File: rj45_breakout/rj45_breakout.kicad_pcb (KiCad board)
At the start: 2 copper layers, 74.3 x 80.6 mm, 19 parts, among them J10 Conn_01x08, J6 RJ45_Shielded, J9 Conn_02x04_Odd_Even

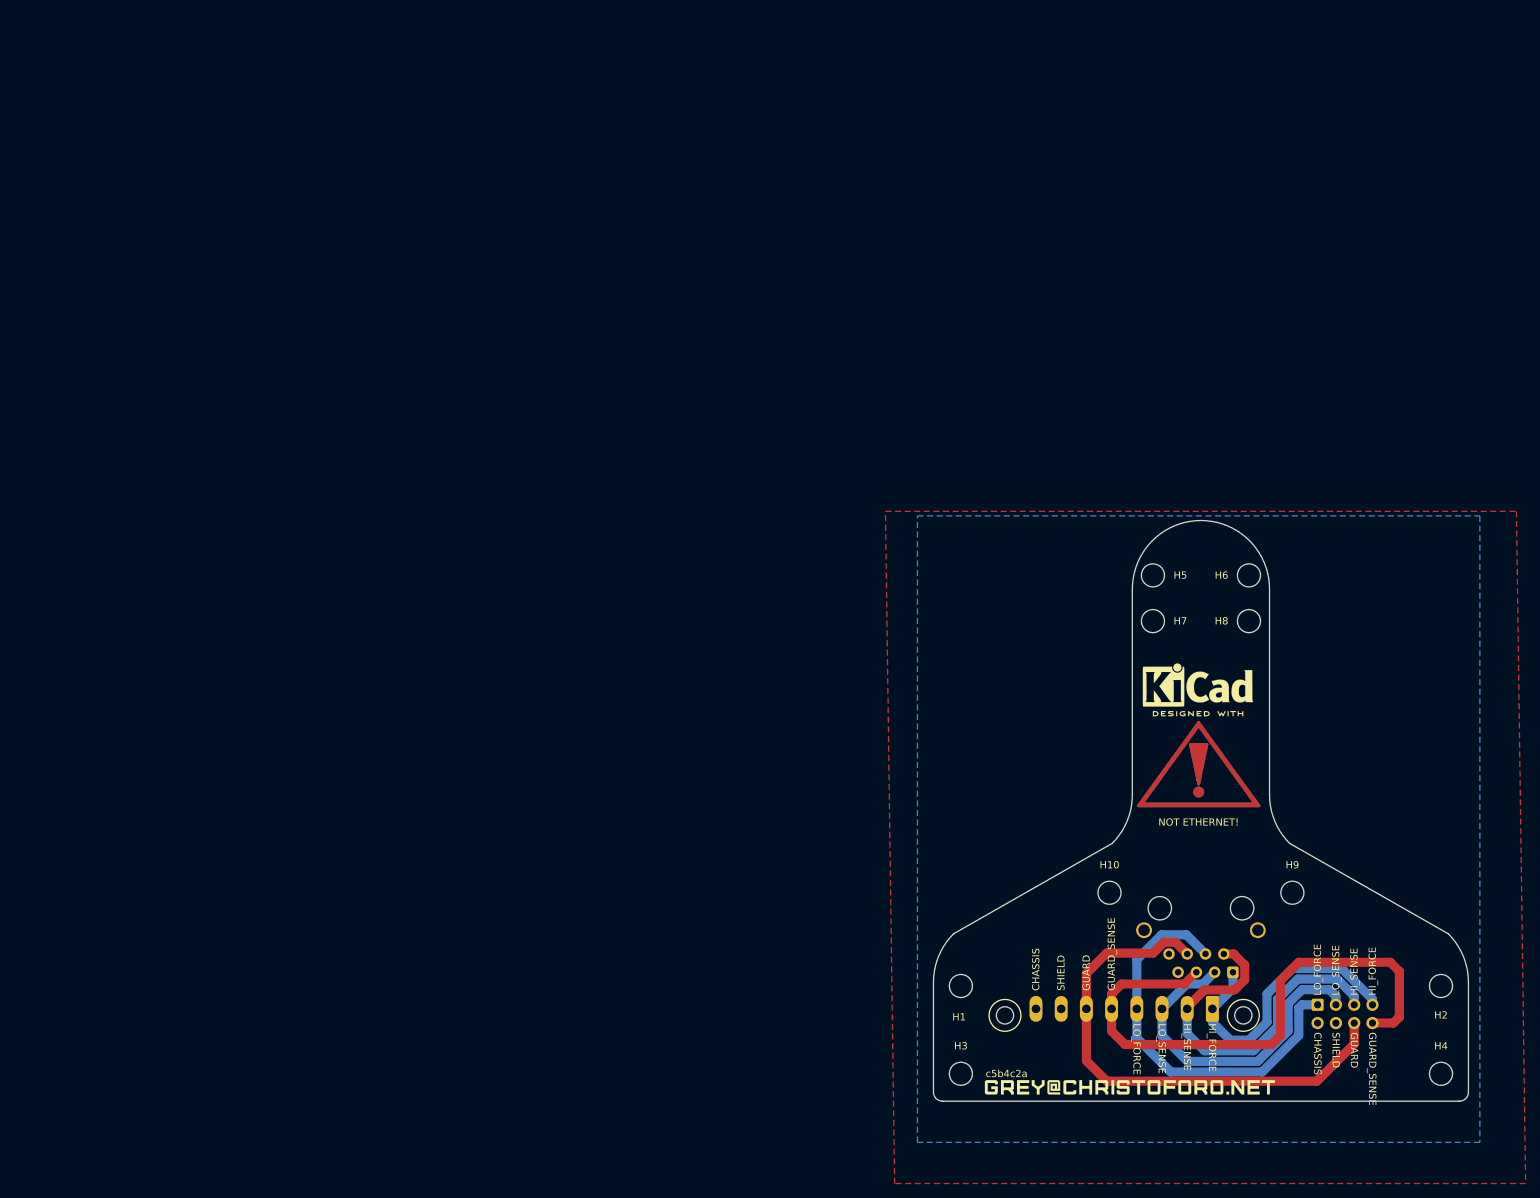
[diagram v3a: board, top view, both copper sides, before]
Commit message: move connector to edge
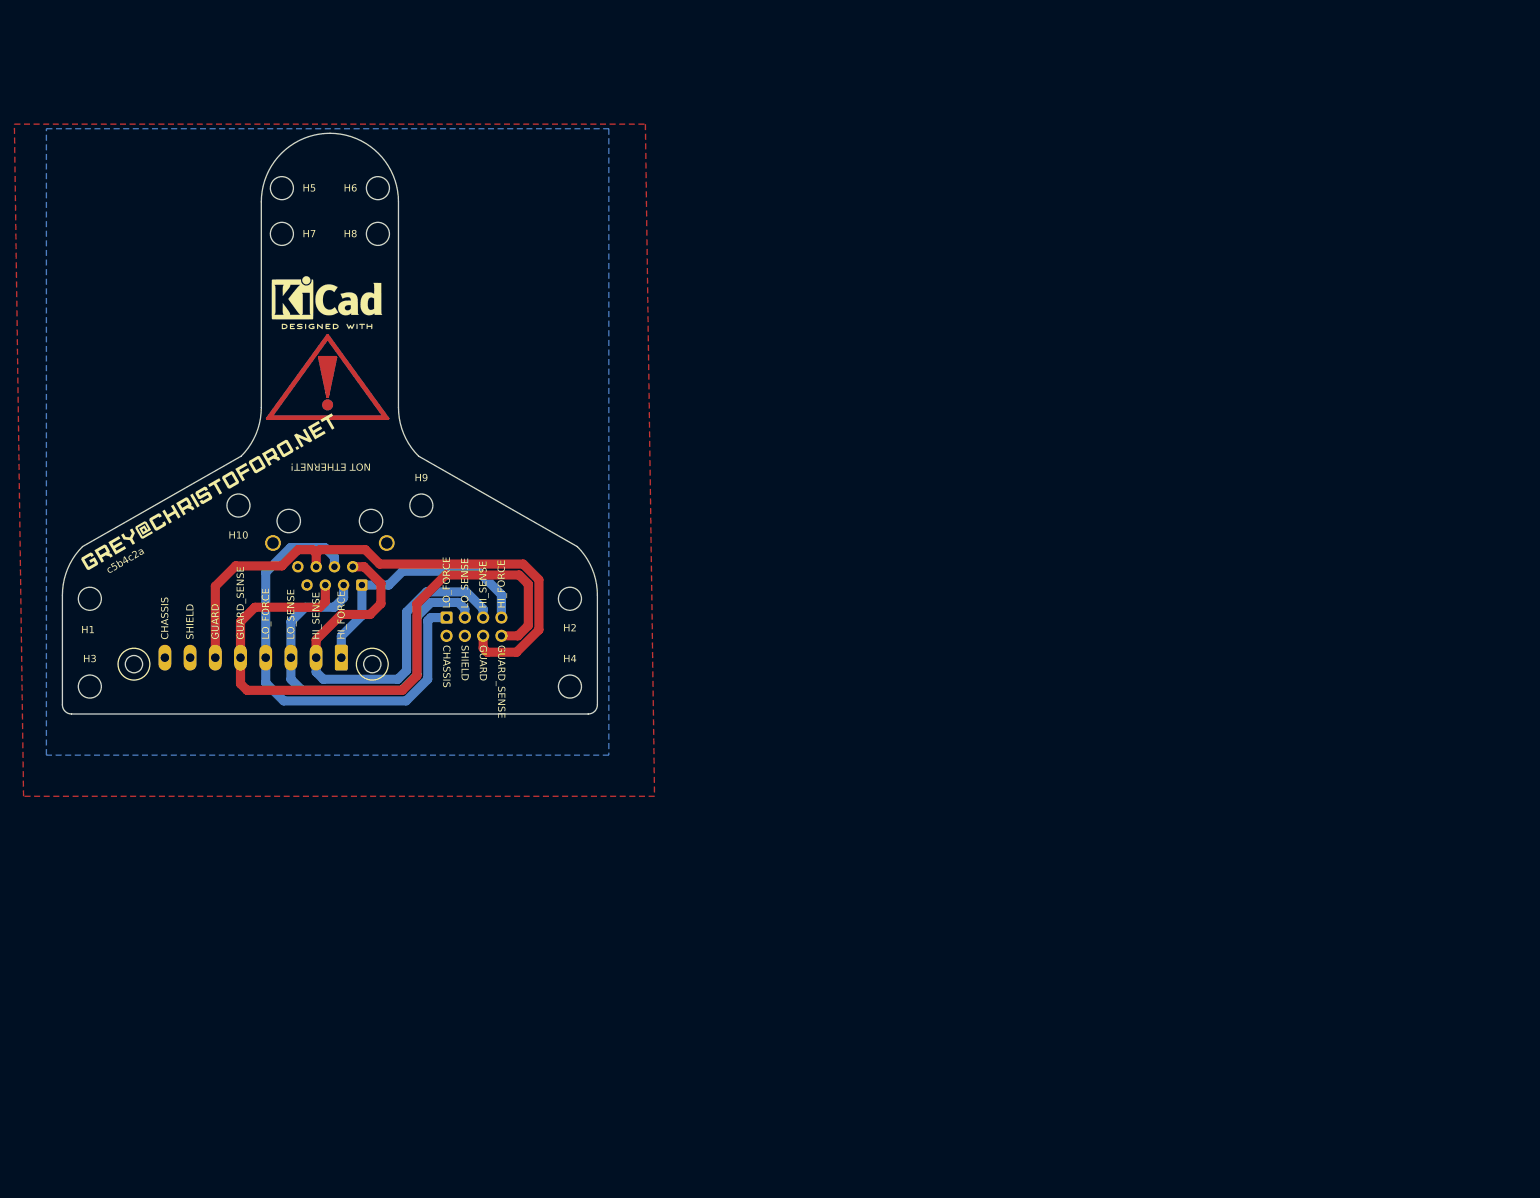
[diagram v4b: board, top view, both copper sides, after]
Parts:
- removed the REF** at (119.0, 3.77) (x2)
- removed the REF** at (119.1, 15.9) (x2)
- added REF**: Symbol_Attention_CopperTop_Big, Symbol:Symbol_Attention_CopperTop_Big, F.Cu at (-1.91, -37.9)
- added REF**: KiCad-Logo2_6mm_SilkScreen, Symbol:KiCad-Logo2_6mm_SilkScreen, F.Cu at (-2.00, -50.0)
- added REF**: KiCad-Logo2_6mm_SilkScreen, Symbol:KiCad-Logo2_6mm_SilkScreen, B.Cu at (-2.00, -50.0)
- added REF**: Symbol_Attention_CopperTop_Big, Symbol:Symbol_Attention_CopperTop_Big, B.Cu at (-1.91, -37.9)
- moved LOGO1 152.4 mm to (-18.5, -23.0), turned to -150 degrees
- moved LOGO2 152.2 mm to (-18.2, -23.0), turned to 30 degrees
- moved H1 132.4 mm to (-34.9, -8.18)
- moved H10 132.4 mm to (-14.3, -21.1)
- moved H2 132.4 mm to (31.8, -8.18)
- moved H3 132.4 mm to (-34.9, 4.01)
- moved H4 132.4 mm to (31.8, 4.01)
- moved H5 132.4 mm to (-8.26, -65.2)
- moved H6 132.4 mm to (5.08, -65.2)
- moved H7 132.4 mm to (-8.26, -58.9)
- moved H8 132.4 mm to (5.08, -58.9)
- moved H9 132.4 mm to (11.1, -21.1)
- moved J6 132.4 mm to (-1.59, -16.0)
- moved J9 132.4 mm to (14.6, -5.57)
- moved J10 130.4 mm to (0.00, 0.00)
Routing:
- net /GUARD_SENSE: track 79.1 -> 87.3 mm
- net /LO_SENSE: track 46.7 -> 54.6 mm
- net /LO_FORCE: track 56.1 -> 63.9 mm
- net /HI_SENSE: track 51.5 -> 58.8 mm
- net /GUARD: track 72.0 -> 78.9 mm
- net /HI_FORCE: track 40.3 -> 36.0 mm

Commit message: update silk
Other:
- board text added: "f207ca1"
- board text removed: "c5b4c2a"
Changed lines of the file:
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@@
     (effects (font (size 1 1) (thickness 0.15)) (justify right mirror))
   )
-  (gr_text "c5b4c2a" (at -30 -13.5 30) (layer "B.SilkS")
+  (gr_text "f207ca1" (at -30 -13.5 30) (layer "B.SilkS")
     (effects (font (size 1 1) (thickness 0.15)) (justify mirror))
   )
@@
     (effects (font (size 1 1) (thickness 0.15)) (justify left))
   )
-  (gr_text "c5b4c2a" (at -30 -13.5 30) (layer "F.SilkS")
+  (gr_text "f207ca1" (at -30 -13.5 30) (layer "F.SilkS")
     (effects (font (size 1 1) (thickness 0.15)))
   )

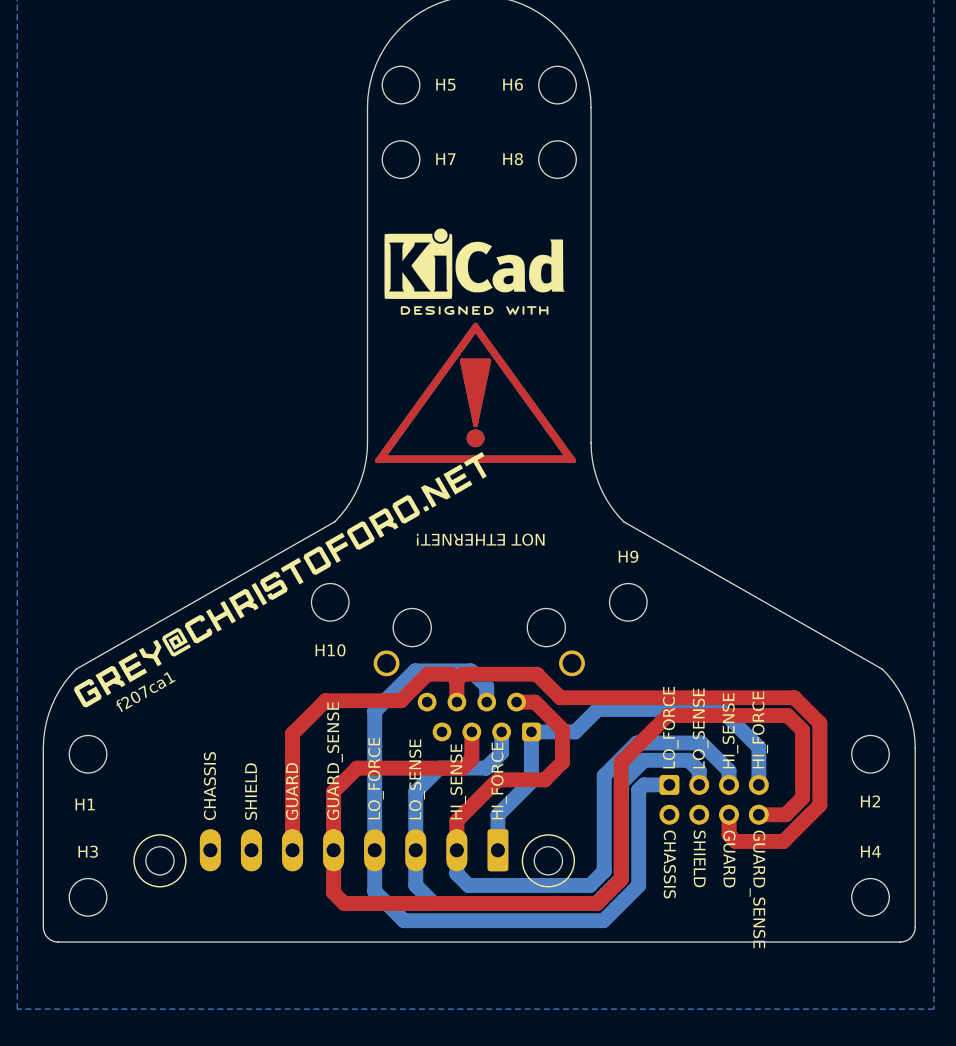
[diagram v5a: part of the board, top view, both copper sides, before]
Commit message: fix up rj45 pad numbering
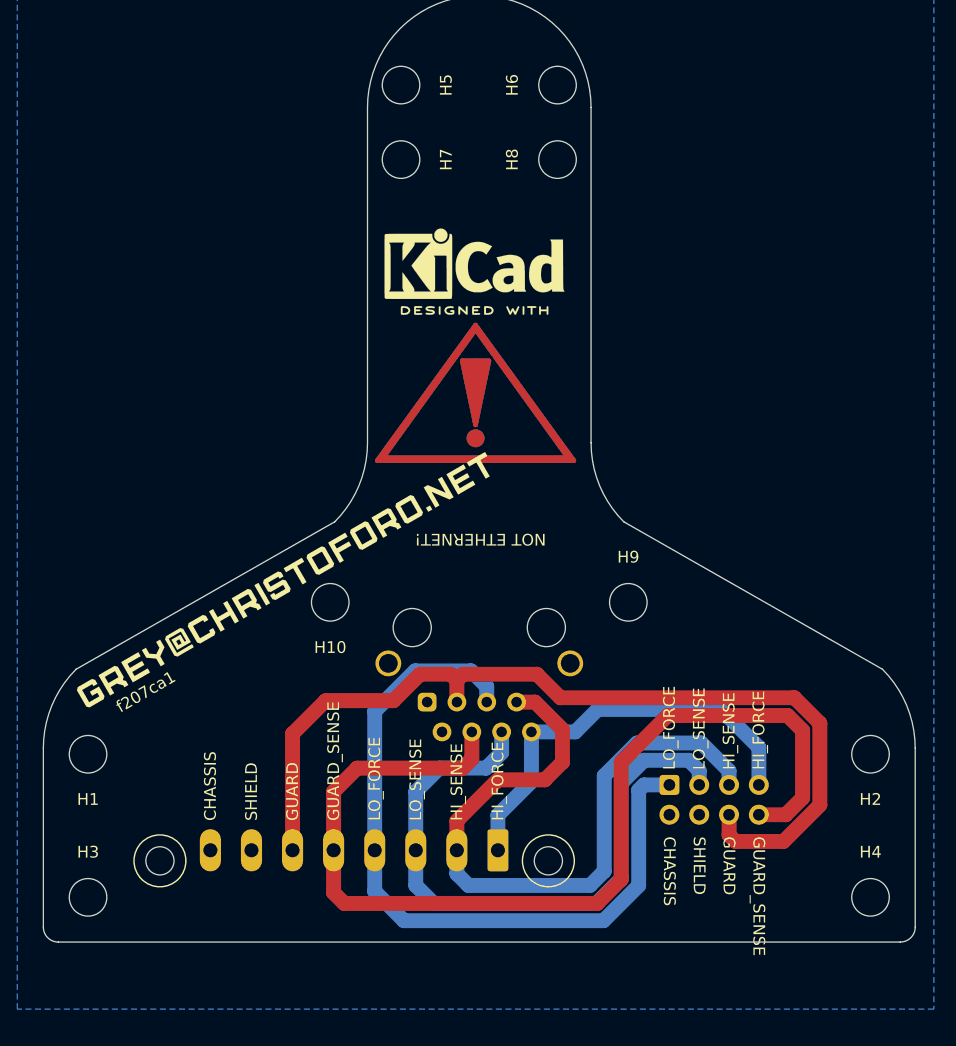
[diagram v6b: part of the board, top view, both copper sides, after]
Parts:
- J6: footprint custom_footprints:RJ45_WURTH_615008142621_horizontal_shield -> custom_footprints:RJ45_WURTH_615008142621
- LOGO1: moved to F.Cu
- LOGO2: moved to B.Cu
- moved LOGO1 0.50 mm to (-18.0, -23.0), turned to 30 degrees
- moved LOGO2 0.25 mm to (-18.0, -23.0)
- turned H1 to 180 degrees
- turned H10 to 180 degrees
- turned H2 to 180 degrees
- turned H5 to -90 degrees
- turned H6 to 90 degrees
- turned H7 to -90 degrees
- turned H8 to 90 degrees
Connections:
- J6 pad 1: /HI_FORCE -> GNDPWR
- J6 pad 2: /HI_SENSE -> GNDPWR
- J6 pad 3: /LO_SENSE -> /GUARD
- J6 pad 4: /LO_FORCE -> /GUARD_SENSE
- J6 pad 5: /GUARD_SENSE -> /LO_FORCE
- J6 pad 6: /GUARD -> /LO_SENSE
- J6 pad 7: GNDPWR -> /HI_SENSE
- J6 pad 8: GNDPWR -> /HI_FORCE

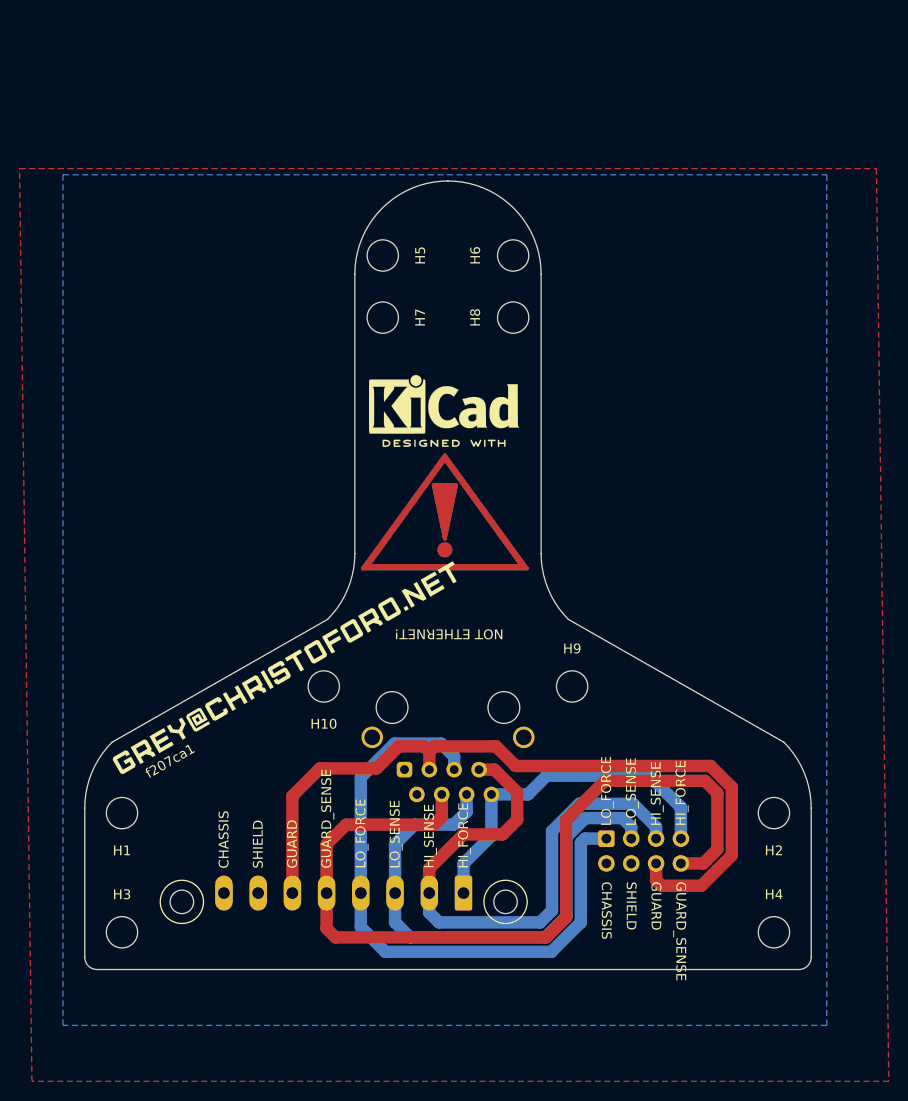
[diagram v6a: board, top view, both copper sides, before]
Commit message: shrink steps, add double rj45 to cc
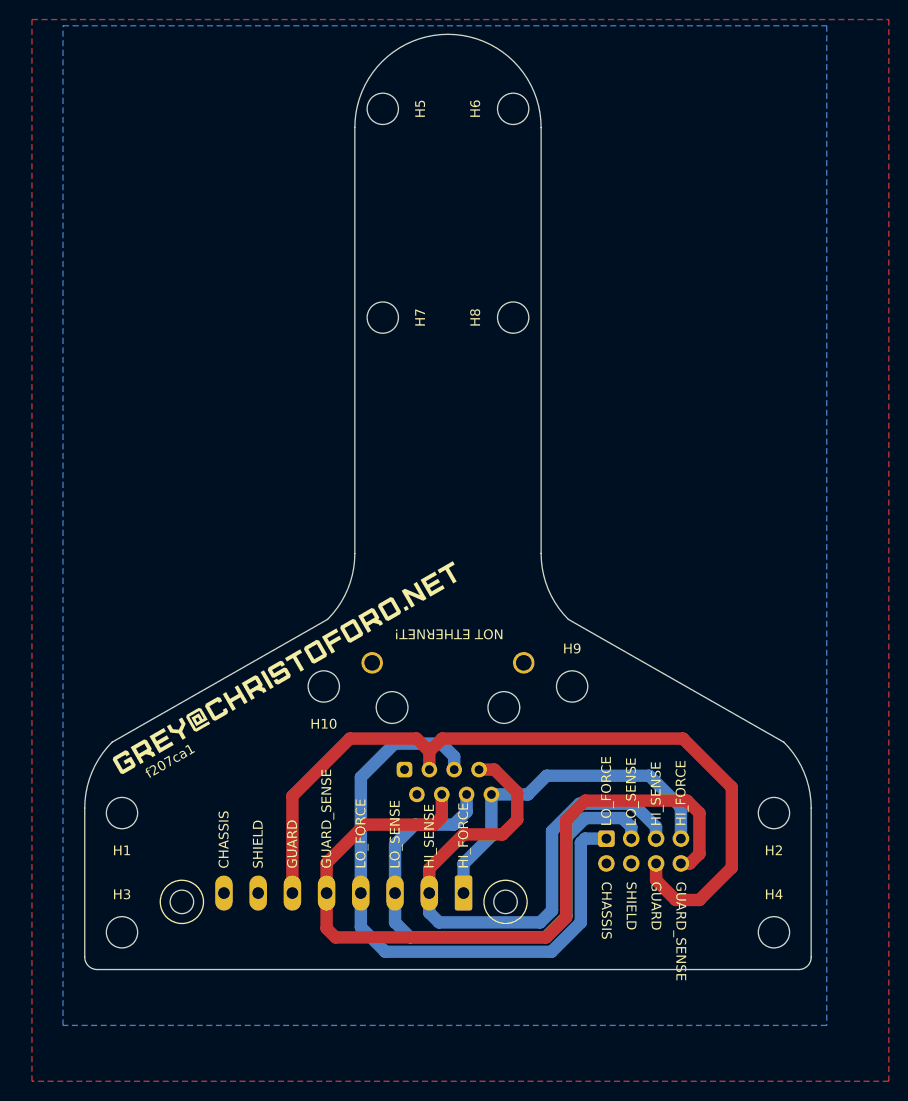
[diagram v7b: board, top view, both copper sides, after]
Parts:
- removed REF** (x2): Symbol_Attention_CopperTop_Big, Symbol:Symbol_Attention_CopperTop_Big
- removed REF** (x2): KiCad-Logo2_6mm_SilkScreen, Symbol:KiCad-Logo2_6mm_SilkScreen
- J6: footprint custom_footprints:RJ45_WURTH_615008142621 -> custom_footprints:RJ45_WURTH_61500814221
- moved H5 15.0 mm to (-8.26, -80.2)
- moved H6 15.0 mm to (5.08, -80.2)
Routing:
- net /GUARD_SENSE: track 87.3 -> 79.9 mm
- net /GUARD: track 78.9 -> 82.2 mm
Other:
- board size 74.3 x 80.6 mm -> 74.3 x 95.6 mm

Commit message: update silk
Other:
- board text added: "193bdad"
- board text removed: "f207ca1"
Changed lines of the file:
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@@
     (effects (font (size 1 1) (thickness 0.15)) (justify right mirror))
   )
-  (gr_text "f207ca1" (at -30 -13.5 -150) (layer "B.SilkS")
+  (gr_text "193bdad" (at -30 -13.5 210) (layer "B.SilkS")
     (effects (font (size 1 1) (thickness 0.15)) (justify mirror))
   )
@@
     (effects (font (size 1 1) (thickness 0.15)) (justify left))
   )
-  (gr_text "f207ca1" (at -30 -13.5 30) (layer "F.SilkS")
+  (gr_text "193bdad" (at -30 -13.5 30) (layer "F.SilkS")
     (effects (font (size 1 1) (thickness 0.15)))
   )
